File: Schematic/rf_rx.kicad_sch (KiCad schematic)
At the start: 7 parts, among them U1 ME6217C33M5G, U12 E28-2G4M27SX

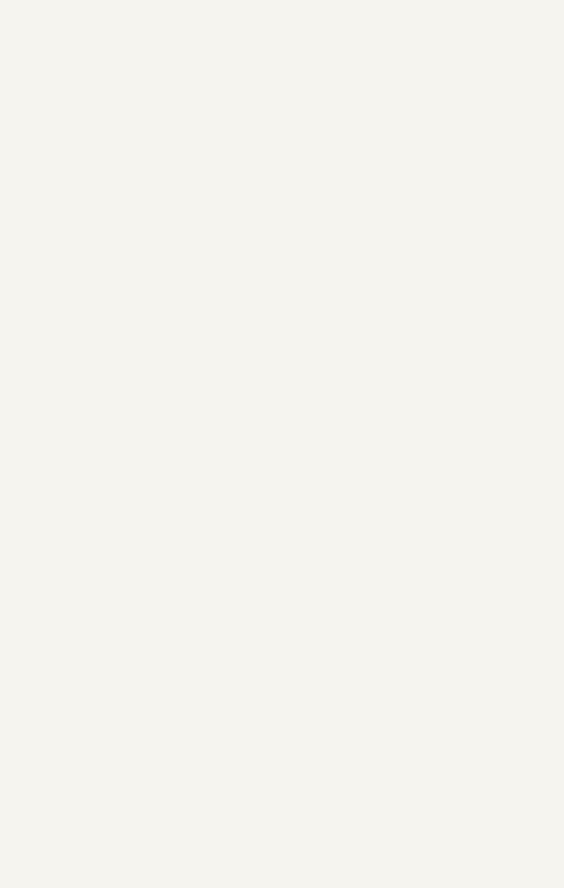
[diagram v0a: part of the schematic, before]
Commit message: Update schematic files and footprint references
- Updated the footprint reference in `fp-info-cache` for various components to use "fch7" instead of "fch7_fp".
- Added a new 3D library reference for "fch7_3d" in `fp-lib-table`.
- Introduced a new symbol for the RF GPS module "MIA-M10Q" in `rf_rx.kicad_sch`, including properties such as footprint, datasheet, and description.
- Added multiple pins for the "MIA-M10Q" symbol with unique UUIDs.
- Corrected the URI for the `fclib` in `sym-lib-table` to point to the correct project path.
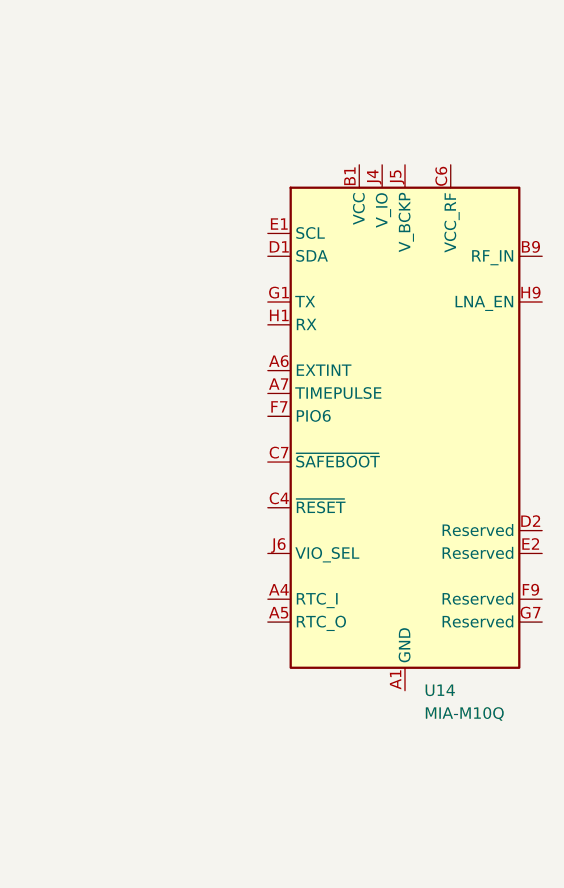
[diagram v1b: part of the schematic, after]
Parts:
- added U14: MIA-M10Q, Package_LGA:ublox_LGA-53_4.5x4.5mm_Layout9x9_P0.5mm, symbol RF_GPS:MIA-M10Q
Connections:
- new net: U14.A1 (GND), U14.A2 (GND), U14.A3 (GND), U14.A8 (GND), U14.A9 (GND), U14.B2 (GND), U14.B8 (GND), U14.C3 (GND), U14.C9 (GND), U14.E3 (GND), U14.E4 (GND), U14.E9 (GND), U14.F1 (GND), U14.F3 (GND), U14.F4 (GND), U14.G3 (GND), U14.G4 (GND), U14.G5 (GND), U14.G6 (GND), U14.H8 (GND), U14.J8 (GND), U14.J9 (GND)
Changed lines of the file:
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@@
+	)
+	(symbol
+		(lib_id "RF_GPS:MIA-M10Q")
+		(at 204.47 90.17 0)
+		(unit 1)
+		(exclude_from_sim no)
+		(in_bom yes)
+		(on_board yes)
+		(dnp no)
+		(fields_autoplaced yes)
+		(property "Reference" "U14"
+			(at 206.6133 118.11 0)
+			(effects
+				(font
+					(size 1.27 1.27)
+				)
+				(justify left)
+			)
+		)
+		(property "Value" "MIA-M10Q"
+			(at 206.6133 120.65 0)
+			(effects
+				(font
+					(size 1.27 1.27)
+				)
+				(justify left)
+			)
+		)
+		(property "Footprint" "Package_LGA:ublox_LGA-53_4.5x4.5mm_Layout9x9_P0.5mm"
+			(at 204.47 90.17 0)
+			(effects
+				(font
+					(size 1.27 1.27)
+				)
+				(hide yes)
+			)
+		)
+		(property "Datasheet" "https://content.u-blox.com/sites/default/files/documents/MIA-M10Q_DataSheet_UBX-22015849.pdf"
+			(at 204.47 90.17 0)
+			(effects
+				(font
+					(size 1.27 1.27)
+				)
+				(hide yes)
+			)
+		)
+		(property "Description" "GNSS receiver module (GPS, Galileo, GLONASS, BeiDou), I2C / UART interface, LGA-53 (MIA M-LGA53)"
+			(at 204.47 90.17 0)
+			(effects
+				(font
+					(size 1.27 1.27)
+				)
+				(hide yes)
+			)
+		)
+		(pin "A9"
+		)
+		(pin "A3"
+		)
+		(pin "C3"
+		)
+		(pin "A8"
+		)
+		(pin "C9"
+		)
+		(pin "B2"
+		)
+		(pin "E9"
+		)
+		(pin "B8"
+		)
+		(pin "F1"
+		)
+		(pin "E3"
+		)
+		(pin "G3"
+		)
+		(pin "E4"
+		)
+		(pin "G4"
+		)
+		(pin "F3"
+		)
+		(pin "H8"
+		)
+		(pin "F4"
+		)
+		(pin "J8"
+		)
+		(pin "G5"
+		)
+		(pin "C1"
+		)
+		(pin "G6"
+		)
+		(pin "C5"
+		)
+		(pin "J9"
+		)
+		(pin "D9"
+		)
+		(pin "C6"
+		)
+		(pin "F9"
+		)
+		(pin "E7"
+		)
+		(pin "J2"
+		)
+		(pin "J3"
+		)
+		(pin "D2"
+		)
+		(pin "H9"
+		)
+		(pin "J7"
+		)
+		(pin "J1"
+		)
+		(pin "G7"
+		)
+		(pin "E2"
+		)
+		(pin "B9"
+		)
+		(pin "G9"
+		)
+		(pin "E1"
+		)
+		(pin "H1"
+		)
+		(pin "J6"
+		)
+		(pin "C4"
+		)
+		(pin "F7"
+		)
+		(pin "C7"
+		)
+		(pin "A7"
+		)
+		(pin "A6"
+		)
+		(pin "G1"
+		)
+		(pin "D1"
+		)
+		(pin "B1"
+		)
+		(pin "J4"
+		)
+		(pin "A4"
+		)
+		(pin "A5"
+		)
+		(pin "A1"
+		)
+		(pin "A2"
+		)
+		(pin "J5"
+		)
+		(instances
+			(project ""
+				(path "/11716af6-0e6e-444b-b738-3f12da23c1a2/c005db94-b190-4389-8874-35307c577c05"
+					(reference "U14")
+					(unit 1)
+				)
+			)
+		)
 	)
 	(symbol

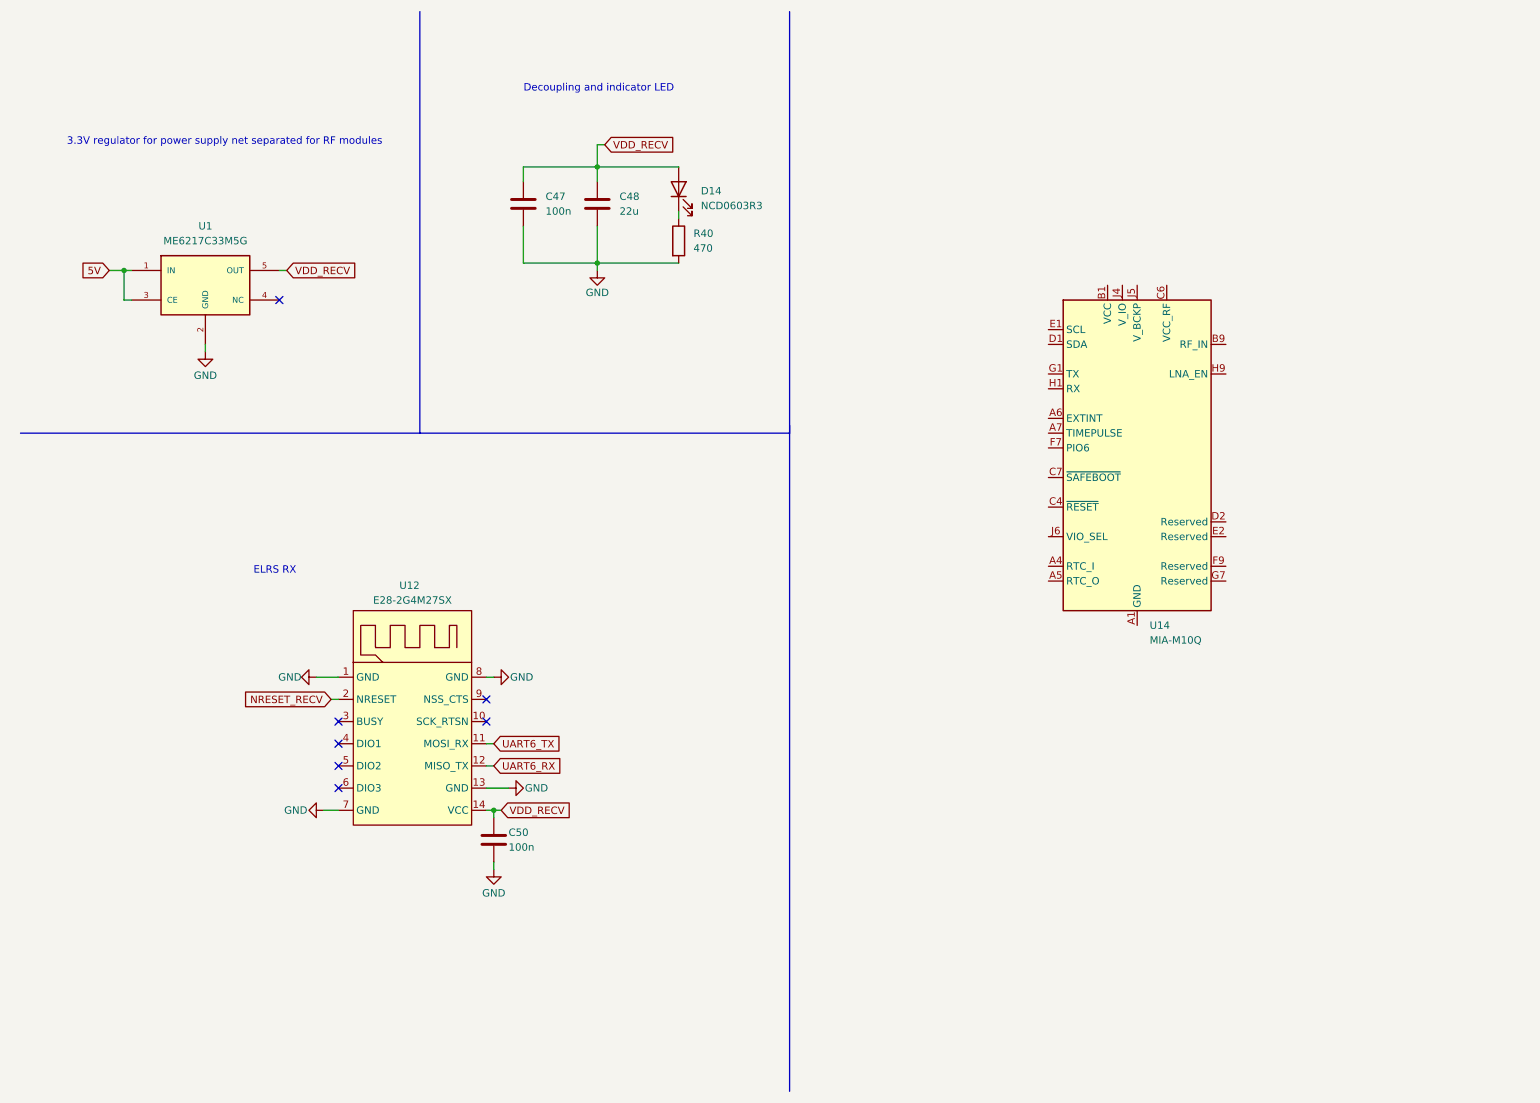
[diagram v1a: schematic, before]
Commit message: update routing and add MIA-M10Q
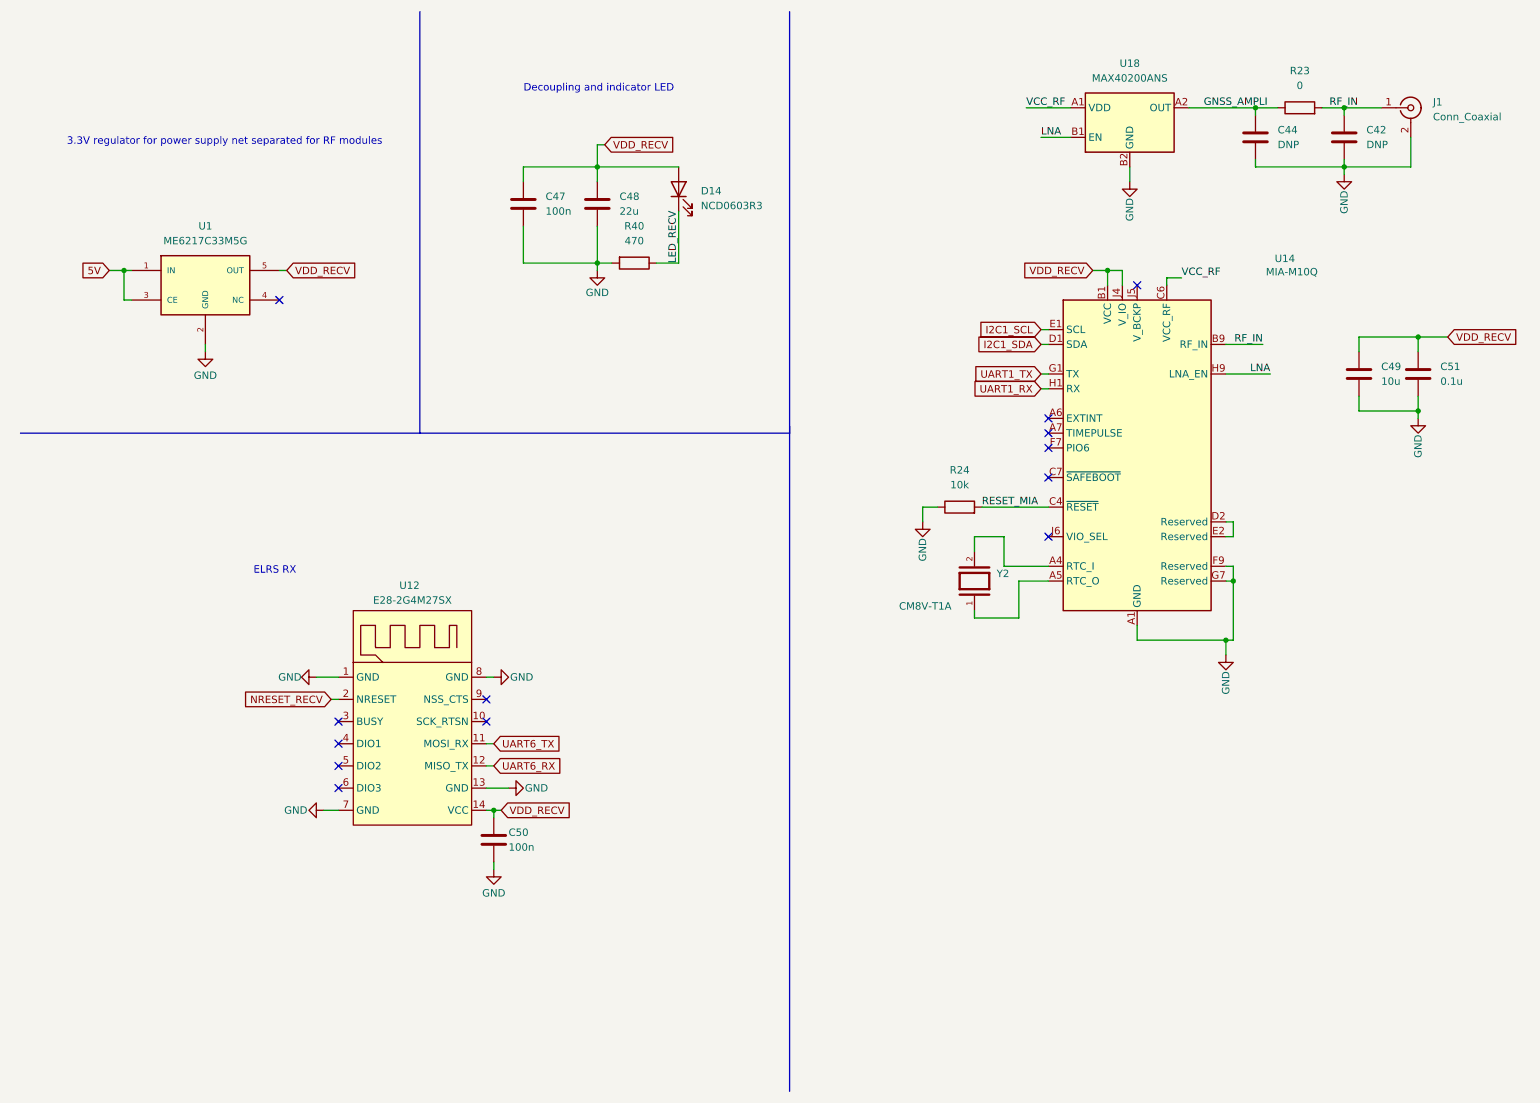
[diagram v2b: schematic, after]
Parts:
- added C42, C44: DNP, Capacitor_SMD:C_0603_1608Metric, symbol Device:C
- added C49: 10u, Capacitor_SMD:C_0402_1005Metric, symbol Device:C
- added C51: 0.1u, Capacitor_SMD:C_0402_1005Metric, symbol Device:C
- added J1: Conn_Coaxial, fch7:AMPHENOL_A-1JB, symbol Connector:Conn_Coaxial
- added R23: 0, Resistor_SMD:R_0603_1608Metric, symbol Device:R
- added R24: 10k, Resistor_SMD:R_0603_1608Metric, symbol Device:R
- added U18: MAX40200ANS, Package_BGA:WLP-4_0.728x0.728mm_Layout2x2_P0.35mm, symbol Analog_Switch:MAX40200ANS
- added Y2: CM8V-T1A, fch7:XTAL_CM8V-T1A-32.768KHZ-7PF-20PPM-TB-QC, symbol fclib:CM8V-T1A-32.768KHZ-7PF-20PPM-TB-QC
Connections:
- net GND: now also U14.A1 (GND), U14.A2 (GND), U14.A3 (GND), U14.A8 (GND), U14.A9 (GND), U14.B2 (GND), U14.B8 (GND), U14.C3 (GND), U14.C9 (GND), U14.E3 (GND), U14.E4 (GND), U14.E9 (GND), U14.F1 (GND), U14.F3 (GND), U14.F4 (GND), U14.F9 (Reserved), U14.G3 (GND), U14.G4 (GND), U14.G5 (GND), U14.G6 (GND), U14.G7 (Reserved), U14.H8 (GND), U14.J8 (GND), U14.J9 (GND), C42.2, C44.2, C49.2, C51.2, J1.2 (Ext), R24.1, U18.B2 (GND)
- net VDD_RECV: now also U14.B1 (VCC), U14.J4 (V_IO), C49.1, C51.1
- net at U14.A4 (RTC_I): now also Y2.2
- net at U14.A5 (RTC_O): now also Y2.1
- net RF_IN: now reaches U14.B9 (RF_IN)
- net RF_IN: now also C42.1, J1.1 (In), R23.2
- net RESET_MIA: now reaches U14.C4 (~{RESET})
- net RESET_MIA: now also R24.2
- net VCC_RF: now reaches U14.C6 (VCC_RF)
- net VCC_RF: now also U18.A1 (VDD)
- net I2C1_SDA: now reaches U14.D1 (SDA)
- net at U14.D2 (Reserved): now also U14.E2 (Reserved)
- net I2C1_SCL: now reaches U14.E1 (SCL)
- net UART1_TX: now reaches U14.G1 (TX)
- net UART1_RX: now reaches U14.H1 (RX)
- net LNA: now reaches U14.H9 (LNA_EN)
- net LNA: now also U18.B1 (EN)
- net LED_RECV: now reaches D14.1 (K), R40.1
- new net GNSS_AMPLI: C44.1, R23.1, U18.A2 (OUT)
- no-connect marks 7 -> 13
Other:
- moved on the sheet: R40

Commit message: update routing
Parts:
- removed J1: Conn_Coaxial, fch7:AMPHENOL_A-1JB, symbol Connector:Conn_Coaxial
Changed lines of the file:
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@@
 	)
 	(junction
-		(at 240.03 29.21)
+		(at 219.71 120.65)
 		(diameter 0)
 		(color 0 0 0 0)
 	)
 	(junction
-		(at 219.71 120.65)
+		(at 252.73 68.58)
 		(diameter 0)
 		(color 0 0 0 0)
 	)
 	(junction
-		(at 252.73 68.58)
+		(at 240.03 29.21)
 		(diameter 0)
 		(color 0 0 0 0)
@@
 	(wire
 		(pts
-			(xy 209.55 58.42) (xy 212.09 58.42)
+			(xy 209.55 58.42) (xy 217.17 58.42)
 		)
 		(stroke
@@
 	(wire
 		(pts
+			(xy 240.03 30.48) (xy 240.03 29.21)
+		)
+		(stroke
+			(width 0)
+			(type default)
+		)
+	)
+	(wire
+		(pts
 			(xy 93.98 158.75) (xy 93.98 160.02)
 		)
@@
 	(wire
 		(pts
-			(xy 240.03 39.37) (xy 240.03 40.64)
+			(xy 240.03 29.21) (xy 246.38 29.21)
 		)
 		(stroke
@@
 	(wire
 		(pts
-			(xy 252.73 68.58) (xy 242.57 68.58)
+			(xy 240.03 39.37) (xy 240.03 40.64)
 		)
 		(stroke
@@
 	(wire
 		(pts
-			(xy 242.57 78.74) (xy 242.57 81.28)
+			(xy 252.73 68.58) (xy 242.57 68.58)
 		)
 		(stroke
@@
 	(wire
 		(pts
-			(xy 240.03 29.21) (xy 246.38 29.21)
+			(xy 242.57 78.74) (xy 242.57 81.28)
 		)
 		(stroke
@@
 	(wire
 		(pts
-			(xy 236.22 29.21) (xy 240.03 29.21)
-		)
-		(stroke
-			(width 0)
-			(type default)
-		)
-	)
-	(wire
-		(pts
 			(xy 92.71 127) (xy 93.98 127)
 		)
@@
 	(wire
 		(pts
-			(xy 219.71 74.93) (xy 227.33 74.93)
+			(xy 219.71 74.93) (xy 224.79 74.93)
 		)
 		(stroke
@@
 	(wire
 		(pts
+			(xy 236.22 29.21) (xy 240.03 29.21)
+		)
+		(stroke
+			(width 0)
+			(type default)
+		)
+	)
+	(wire
+		(pts
 			(xy 111.76 39.37) (xy 125.73 39.37)
 		)
@@
 	(wire
 		(pts
-			(xy 240.03 29.21) (xy 240.03 30.48)
-		)
-		(stroke
-			(width 0)
-			(type default)
-		)
-	)
-	(wire
-		(pts
 			(xy 219.71 107.95) (xy 220.98 107.95)
 		)
@@
 	)
 	(label "LNA"
-		(at 227.33 74.93 180)
+		(at 224.79 74.93 180)
 		(effects
 			(font
@@
 	)
 	(label "VCC_RF"
-		(at 212.09 58.42 0)
+		(at 217.17 58.42 180)
 		(effects
 			(font
 				(size 1.27 1.27)
 			)
-			(justify left bottom)
+			(justify right bottom)
 		)
 	)
@@
 					(unit 1)
 				)
-			)
-		)
-	)
-	(symbol
-		(lib_id "Connector:Conn_Coaxial")
-		(at 251.46 29.21 0)
-		(unit 1)
-		(exclude_from_sim no)
-		(in_bom yes)
-		(on_board yes)
-		(dnp no)
-		(fields_autoplaced yes)
-		(property "Reference" "J1"
-			(at 255.27 28.2331 0)
-			(effects
-				(font
-					(size 1.27 1.27)
-				)
-				(justify left)
-			)
-		)
-		(property "Value" "Conn_Coaxial"
-			(at 255.27 30.7731 0)
-			(effects
-				(font
-					(size 1.27 1.27)
-				)
-				(justify left)
-			)
-		)
-		(property "Footprint" "fch7:AMPHENOL_A-1JB"
-			(at 251.46 29.21 0)
-			(effects
-				(font
-					(size 1.27 1.27)
-				)
-				(hide yes)
-			)
-		)
-		(property "Datasheet" "~"
-			(at 251.46 29.21 0)
-			(effects
-				(font
-					(size 1.27 1.27)
-				)
-				(hide yes)
-			)
-		)
-		(property "Description" "coaxial connector (BNC, SMA, SMB, SMC, Cinch/RCA, LEMO, ...)"
-			(at 251.46 29.21 0)
-			(effects
-				(font
-					(size 1.27 1.27)
-				)
-				(hide yes)
-			)
-		)
-		(pin "2"
-		)
-		(pin "1"
-		)
-		(instances
-			(project ""
-				(path "/11716af6-0e6e-444b-b738-3f12da23c1a2/c005db94-b190-4389-8874-35307c577c05"
-					(reference "J1")
-					(unit 1)
-				)

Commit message: update routing
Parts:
- added J1: U.FL-R-SMT-1_01_, fch7:HIROSE_U.FL-R-SMT-1_01_, symbol fclib:U.FL-R-SMT-1_01_
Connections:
- net GND: now also J1.G1, J1.G2
- net RF_IN: now also J1.SIG
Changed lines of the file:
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@@
 	(wire
 		(pts
-			(xy 240.03 39.37) (xy 251.46 39.37)
+			(xy 240.03 39.37) (xy 245.11 39.37)
 		)
 		(stroke
@@
 	(wire
 		(pts
+			(xy 246.38 31.75) (xy 245.11 31.75)
+		)
+		(stroke
+			(width 0)
+			(type default)
+		)
+	)
+	(wire
+		(pts
 			(xy 252.73 78.74) (xy 252.73 81.28)
 		)
@@
 	(wire
 		(pts
-			(xy 251.46 39.37) (xy 251.46 34.29)
-		)
-		(stroke
-			(width 0)
-			(type default)
-		)
-	)
-	(wire
-		(pts
 			(xy 99.06 39.37) (xy 99.06 41.91)
 		)
@@
 	(wire
 		(pts
+			(xy 245.11 31.75) (xy 245.11 39.37)
+		)
+		(stroke
+			(width 0)
+			(type default)
+		)
+	)
+	(wire
+		(pts
 			(xy 196.85 57.15) (xy 199.39 57.15)
 		)
@@
 					(unit 1)
 				)
+			)
+		)
+	)
+	(symbol
+		(lib_id "fclib:U.FL-R-SMT-1_01_")
+		(at 248.92 29.21 0)
+		(unit 1)
+		(exclude_from_sim no)
+		(in_bom yes)
+		(on_board yes)
+		(dnp no)
+		(property "Reference" "J1"
+			(at 250.19 35.306 0)
+			(effects
+				(font
+					(size 1.27 1.27)
+				)
+				(justify left)
+			)
+		)
+		(property "Value" "U.FL-R-SMT-1_01_"
+			(at 246.126 25.654 0)
+			(effects
+				(font
+					(size 1.27 1.27)
+				)
+				(justify left)
+			)
+		)
+		(property "Footprint" "fch7:HIROSE_U.FL-R-SMT-1_01_"
+			(at 249.936 41.656 0)
+			(effects
+				(font
+					(size 1.27 1.27)
+				)
+				(justify bottom)
+				(hide yes)
+			)
+		)
+		(property "Datasheet" ""
+			(at 248.92 29.21 0)
+			(effects
+				(font
+					(size 1.27 1.27)
+				)
+				(hide yes)
+			)
+		)
+		(property "Description" ""
+			(at 248.92 29.21 0)
+			(effects
+				(font
+					(size 1.27 1.27)
+				)
+				(hide yes)
+			)
+		)
+		(property "DigiKey_Part_Number" "26-U.FL-R-SMT-1(01)-ND"
+			(at 249.174 25.654 0)
+			(effects
+				(font
+					(size 1.27 1.27)
+				)
+				(justify bottom)
+				(hide yes)
+			)
+		)
+		(property "SnapEDA_Link" "https://www.snapeda.com/parts/U.FL-R-SMT-1(01)/Hirose/view-part/?ref=snap"
+			(at 250.444 39.624 0)
+			(effects
+				(font
+					(size 1.27 1.27)
+				)
+				(justify bottom)
+				(hide yes)
+			)
+		)
+		(property "MAXIMUM_PACKAGE_HEIGHT" "1.45mm"
+			(at 256.032 27.94 0)
+			(effects
+				(font
+					(size 1.27 1.27)
+				)
+				(justify bottom)
+				(hide yes)
+			)
+		)
+		(property "Package" "None"
+			(at 248.92 29.21 0)
+			(effects
+				(font
+					(size 1.27 1.27)
+				)
+				(justify bottom)
+				(hide yes)
+			)
+		)
+		(property "Check_prices" "https://www.snapeda.com/parts/U.FL-R-SMT-1(01)/Hirose/view-part/?ref=eda"
+			(at 249.936 22.098 0)
+			(effects
+				(font
+					(size 1.27 1.27)
+				)
+				(justify bottom)
+				(hide yes)
+			)
+		)
+		(property "STANDARD" "Manufacturer Recommendations"
+			(at 248.666 20.574 0)
+			(effects
+				(font
+					(size 1.27 1.27)
+				)
+				(justify bottom)
+				(hide yes)
+			)
+		)
+		(property "PARTREV" "Jul.1.2022"
+			(at 248.158 18.542 0)
+			(effects
+				(font
+					(size 1.27 1.27)
+				)
+				(justify bottom)
+				(hide yes)
+			)
+		)
+		(property "MF" "Hirose"
+			(at 248.92 29.21 0)
+			(effects
+				(font
+					(size 1.27 1.27)
+				)
+				(justify bottom)
+				(hide yes)
+			)
+		)
+		(property "MP" "U.FL-R-SMT-1(01)"
+			(at 249.682 46.482 0)
+			(effects
+				(font
+					(size 1.27 1.27)
+				)
+				(justify bottom)
+				(hide yes)
+			)
+		)
+		(property "Description_1" "U.FL (UMCC) Connector Receptacle, Male Pin 50 Ohms Surface Mount Solder"
+			(at 249.428 24.13 0)
+			(effects
+				(font
+					(size 1.27 1.27)
+				)
+				(justify bottom)
+				(hide yes)
+			)
+		)
+		(property "MANUFACTURER" "Hirose"
+			(at 248.92 29.21 0)
+			(effects
+				(font
+					(size 1.27 1.27)
+				)
+				(justify bottom)
+				(hide yes)
+			)
+		)
+		(property "SNAPEDA_PN" "U.FL-R-SMT-1(01)"
+			(at 247.904 44.196 0)
+			(effects
+				(font
+					(size 1.27 1.27)
+				)
+				(justify bottom)
+				(hide yes)
+			)
+		)
+		(pin "G1"
+		)
+		(pin "G2"
+		)
+		(pin "SIG"
+		)
+		(instances
+			(project ""
+				(path "/11716af6-0e6e-444b-b738-3f12da23c1a2/c005db94-b190-4389-8874-35307c577c05"
+					(reference "J1")
+					(unit 1)
+				)
